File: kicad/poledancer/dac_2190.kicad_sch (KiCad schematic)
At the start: 22 parts, among them U6 AD5328

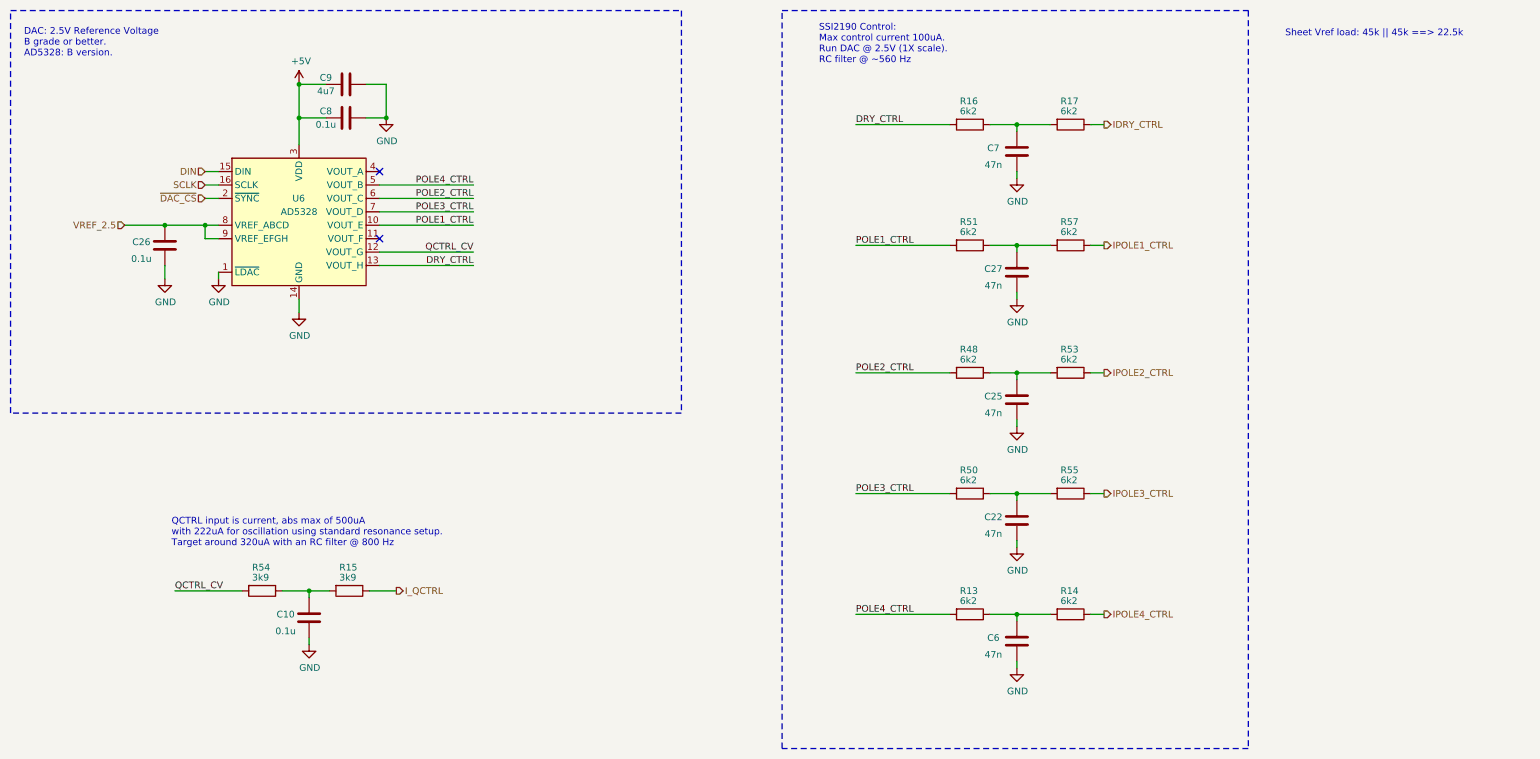
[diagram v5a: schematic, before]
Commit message: add testpoints to DAC2190 for calibration
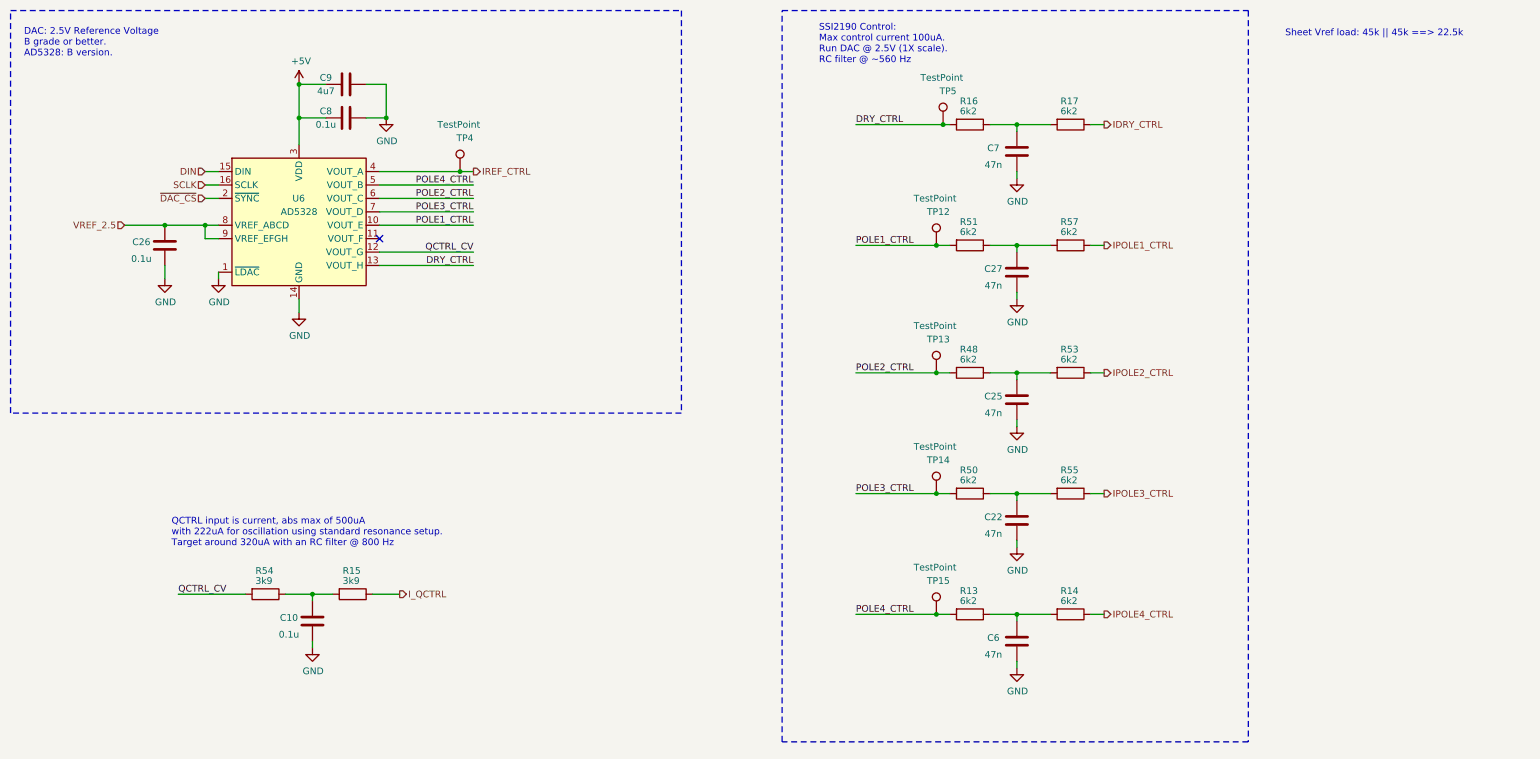
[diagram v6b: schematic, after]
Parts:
- added TP12, TP13, TP14, TP15, TP4, TP5: TestPoint, TestPoint:TestPoint_Pad_2.0x2.0mm, symbol Connector:TestPoint
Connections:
- net DRY_CTRL: now also TP5.1
- net POLE1_CTRL: now also TP12.1
- net POLE2_CTRL: now also TP13.1
- net POLE3_CTRL: now also TP14.1
- net POLE4_CTRL: now also TP15.1
- net IREF_CTRL: now reaches U6.4 (VOUT_A)
- net IREF_CTRL: now also TP4.1
- no-connect marks 2 -> 1
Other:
- moved on the sheet: C10, R15, R54

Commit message: poledancer v0.3 RTM check
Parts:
- renumbered TP5 to TP10, TP12 to TP11, TP13 to TP12, TP14 to TP13, TP15 to TP14, TP4 to TP9
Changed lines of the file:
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@@
   (symbol (lib_id "Connector:TestPoint") (at 196.85 38.1 0) (unit 1)
     (in_bom yes) (on_board yes) (dnp no)
-    (property "Reference" "TP5" (at 199.39 31.75 0)
+    (property "Reference" "TP10" (at 199.39 31.75 0)
       (effects (font (size 1.27 1.27)) (justify right))
     )
@@
       (project "poledancer"
         (path "/7079bdb0-a00e-4bac-b257-cbcf2c91bbd6/57b4b86d-6fc2-4a90-985c-9520b039cd33"
-          (reference "TP5") (unit 1)
+          (reference "TP10") (unit 1)
         )
       )
@@
   (symbol (lib_id "Connector:TestPoint") (at 105.41 46.99 0) (unit 1)
     (in_bom yes) (on_board yes) (dnp no)
-    (property "Reference" "TP4" (at 107.95 40.64 0)
+    (property "Reference" "TP9" (at 107.95 40.64 0)
       (effects (font (size 1.27 1.27)) (justify right))
     )
@@
       (project "poledancer"
         (path "/7079bdb0-a00e-4bac-b257-cbcf2c91bbd6/57b4b86d-6fc2-4a90-985c-9520b039cd33"
-          (reference "TP4") (unit 1)
+          (reference "TP9") (unit 1)
         )
       )
@@
   (symbol (lib_id "Connector:TestPoint") (at 195.58 130.81 0) (unit 1)
     (in_bom yes) (on_board yes) (dnp no)
-    (property "Reference" "TP15" (at 198.12 124.46 0)
+    (property "Reference" "TP14" (at 198.12 124.46 0)
       (effects (font (size 1.27 1.27)) (justify right))
     )
@@
       (project "poledancer"
         (path "/7079bdb0-a00e-4bac-b257-cbcf2c91bbd6/57b4b86d-6fc2-4a90-985c-9520b039cd33"
-          (reference "TP15") (unit 1)
+          (reference "TP14") (unit 1)
         )
       )
@@
   (symbol (lib_id "Connector:TestPoint") (at 195.58 85.09 0) (unit 1)
     (in_bom yes) (on_board yes) (dnp no)
-    (property "Reference" "TP13" (at 198.12 78.74 0)
+    (property "Reference" "TP12" (at 198.12 78.74 0)
       (effects (font (size 1.27 1.27)) (justify right))
     )
@@
       (project "poledancer"
         (path "/7079bdb0-a00e-4bac-b257-cbcf2c91bbd6/57b4b86d-6fc2-4a90-985c-9520b039cd33"
+          (reference "TP12") (unit 1)
+        )
+      )
+    )
+  )
+  (symbol (lib_id "Connector:TestPoint") (at 195.58 107.95 0) (unit 1)
+    (in_bom yes) (on_board yes) (dnp no)
+    (property "Reference" "TP13" (at 198.12 101.6 0)
+      (effects (font (size 1.27 1.27)) (justify right))
+    )
+    (property "Value" "TestPoint" (at 199.39 99.06 0)
+      (effects (font (size 1.27 1.27)) (justify right))
+    )
+    (property "Footprint" "TestPoint:TestPoint_Pad_2.0x2.0mm" (at 200.66 107.95 0)
+      (effects (font (size 1.27 1.27)) hide)
+    )
+    (property "Datasheet" "~" (at 200.66 107.95 0)
+      (effects (font (size 1.27 1.27)) hide)
+    )
+    (pin "1")
+    (instances
+      (project "poledancer"
+        (path "/7079bdb0-a00e-4bac-b257-cbcf2c91bbd6/57b4b86d-6fc2-4a90-985c-9520b039cd33"
           (reference "TP13") (unit 1)
         )
@@
     )
   )
-  (symbol (lib_id "Connector:TestPoint") (at 195.58 107.95 0) (unit 1)
-    (in_bom yes) (on_board yes) (dnp no)
-    (property "Reference" "TP14" (at 198.12 101.6 0)
-      (effects (font (size 1.27 1.27)) (justify right))
-    )
-    (property "Value" "TestPoint" (at 199.39 99.06 0)
-      (effects (font (size 1.27 1.27)) (justify right))
-    )
-    (property "Footprint" "TestPoint:TestPoint_Pad_2.0x2.0mm" (at 200.66 107.95 0)
-      (effects (font (size 1.27 1.27)) hide)
-    )
-    (property "Datasheet" "~" (at 200.66 107.95 0)
-      (effects (font (size 1.27 1.27)) hide)
-    )
-    (pin "1")
-    (instances
-      (project "poledancer"
-        (path "/7079bdb0-a00e-4bac-b257-cbcf2c91bbd6/57b4b86d-6fc2-4a90-985c-9520b039cd33"
-          (reference "TP14") (unit 1)
-        )
-      )
-    )
-  )
   (symbol (lib_id "Device:R") (at 85.09 127 270) (unit 1)
     (in_bom yes) (on_board yes) (dnp no)
@@
   (symbol (lib_id "Connector:TestPoint") (at 195.58 60.96 0) (unit 1)
     (in_bom yes) (on_board yes) (dnp no)
-    (property "Reference" "TP12" (at 198.12 54.61 0)
+    (property "Reference" "TP11" (at 198.12 54.61 0)
       (effects (font (size 1.27 1.27)) (justify right))
     )
@@
       (project "poledancer"
         (path "/7079bdb0-a00e-4bac-b257-cbcf2c91bbd6/57b4b86d-6fc2-4a90-985c-9520b039cd33"
-          (reference "TP12") (unit 1)
-        )
-      )
+          (reference "TP11") (unit 1)
+        )
+      )
